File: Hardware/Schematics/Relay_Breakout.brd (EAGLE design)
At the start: 31 x 40 mm, 14 parts, among them J1 1X2-3.5MM, J2 1X2-3.5MM

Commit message: fixed some issues in relay breakout.
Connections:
- removed net N$2: D4.C, U$2.COIL1
- net +5V: now also D4.C, U$2.COIL1
- net PHASE_OUT: now also U$2.SWCLOSED; no longer U$2.SWOPEN
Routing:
- net +5V: track 56.9 -> 62.7 mm
- net N$2: track 2.60 -> 0.00 mm
- net PHASE: track 12.8 -> 14.7 mm
- net NULL: track 19.6 -> 20.9 mm
- added copper zone on layer 1, net NULL_OUT
- added copper zone on layer 1, net PHASE_OUT
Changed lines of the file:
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@@
 <autorouter>
 <pass name="Default">
-<param name="RoutingGrid" value="50mil"/>
+<param name="RoutingGrid" value="0.25mm"/>
 <param name="AutoGrid" value="1"/>
 <param name="Efforts" value="0"/>
 <param name="TopRouterVariant" value="1"/>
 <param name="tpViaShape" value="round"/>
-<param name="PrefDir.1" value="a"/>
+<param name="PrefDir.1" value="-"/>
 <param name="PrefDir.2" value="0"/>
 <param name="PrefDir.3" value="0"/>
@@
 <param name="PrefDir.14" value="0"/>
 <param name="PrefDir.15" value="0"/>
-<param name="PrefDir.16" value="a"/>
+<param name="PrefDir.16" value="|"/>
 <param name="cfVia" value="8"/>
 <param name="cfNonPref" value="5"/>
@@
 <signal name="PHASE_OUT">
 <contactref element="J2" pad="2"/>
-<contactref element="U$2" pad="SWOPEN"/>
-<polygon width="0.6096" layer="16" thermals="no">
-<vertex x="1.2" y="20.1"/>
-<vertex x="9.8" y="20.1"/>
-<vertex x="9.8" y="23.2"/>
-<vertex x="1.2" y="23.2"/>
+<contactref element="U$2" pad="SWCLOSED"/>
+<polygon width="0.4064" layer="16" thermals="no">
+<vertex x="2.2" y="20"/>
+<vertex x="1.2" y="20"/>
+<vertex x="1.2" y="33.3"/>
+<vertex x="9.4" y="33.3"/>
+<vertex x="9.4" y="28.2"/>
+<vertex x="4.2" y="23"/>
+<vertex x="4.2" y="20"/>
+</polygon>
+<polygon width="0.4064" layer="1" thermals="no">
+<vertex x="4.2" y="20"/>
+<vertex x="1.2" y="20"/>
+<vertex x="1.2" y="33.3"/>
+<vertex x="9.4" y="33.3"/>
+<vertex x="9.4" y="28.2"/>
+<vertex x="4.2" y="23"/>
 </polygon>
 </signal>
@@
 <wire x1="28.470734375" y1="26.7" x2="28.470734375" y2="26.804315625" width="1.016" layer="16"/>
 <wire x1="28.9" y1="26.6" x2="28.9" y2="20.7" width="2.54" layer="16"/>
-<wire x1="27.9" y1="26.7" x2="27.200734375" y2="26.804315625" width="0" layer="19" extent="16-16"/>
-<wire x1="28.9" y1="26.6" x2="28.470734375" y2="26.7" width="0" layer="19" extent="16-16"/>
+<wire x1="27.178" y1="26.797" x2="27.200734375" y2="26.804315625" width="0.127" layer="16"/>
+<wire x1="27.178" y1="26.797" x2="27.9" y2="26.7" width="0.127" layer="16"/>
+<wire x1="27.813" y1="20.574" x2="27.85" y2="20.54" width="0.127" layer="16"/>
+<wire x1="27.813" y1="20.574" x2="28.9" y2="20.7" width="0.127" layer="16"/>
 </signal>
 <signal name="NULL">
@@
 <wire x1="27.8" y1="16.2" x2="27.8" y2="11.6" width="3.81" layer="1"/>
 <wire x1="27.8" y1="11.6" x2="24" y2="11.6" width="3.81" layer="1"/>
-<wire x1="27.8" y1="11.6" x2="27.8" y2="11.6" width="0" layer="19" extent="1-16"/>
+<wire x1="22.86" y1="11.557" x2="24" y2="11.6" width="0.127" layer="1"/>
+<wire x1="22.86" y1="11.557" x2="22.77" y2="11.62" width="0.127" layer="1"/>
 </signal>
 <signal name="N$24">
@@
 <wire x1="27.9" y1="30.5" x2="18.5" y2="30.5" width="0.6096" layer="1"/>
 <wire x1="18.5" y1="30.5" x2="18.6" y2="30.4" width="0.6096" layer="1"/>
-<wire x1="18.6" y1="30.4" x2="18.6" y2="4.4" width="0.6096" layer="1"/>
+<wire x1="18.6" y1="30.4" x2="18.6" y2="23" width="0.6096" layer="1"/>
+<wire x1="18.6" y1="23" x2="18.6" y2="4.4" width="0.6096" layer="1"/>
 <wire x1="18.6" y1="4.4" x2="17.62" y2="3.42" width="0.6096" layer="1"/>
 <wire x1="17.62" y1="3.42" x2="17.62" y2="2.42" width="0.6096" layer="1"/>
+<contactref element="U$2" pad="COIL1"/>
+<contactref element="D4" pad="C"/>
+<wire x1="20.77" y1="20.8" x2="20.155" y2="21.415" width="0.6096" layer="16"/>
+<wire x1="20.155" y1="21.415" x2="18.42" y2="21.415" width="0.6096" layer="16"/>
+<wire x1="20.8" y1="20.8" x2="18.6" y2="23" width="0.6096" layer="1"/>
+<wire x1="20.828" y1="20.828" x2="20.77" y2="20.8" width="0.127" layer="1"/>
+<wire x1="20.828" y1="20.828" x2="20.8" y2="20.8" width="0.127" layer="1"/>
 </signal>
 <signal name="N$41">
@@
 <vertex x="9.8" y="14.5"/>
 <vertex x="1.3" y="14.5"/>
+</polygon>
+<polygon width="0.4064" layer="1" thermals="no">
+<vertex x="2.2" y="18.3"/>
+<vertex x="9.9" y="18.3"/>
+<vertex x="9.9" y="14.4"/>
+<vertex x="1.2" y="14.4"/>
+<vertex x="1.2" y="18.3"/>
 </polygon>
 </signal>
@@
 <wire x1="20.81" y1="32.84" x2="20.81" y2="34.54" width="0.6096" layer="16"/>
 </signal>
-<signal name="N$2">
-<contactref element="U$2" pad="COIL1"/>
-<contactref element="D4" pad="C"/>
-<wire x1="20.77" y1="20.8" x2="20.155" y2="21.415" width="0.6096" layer="16"/>
-<wire x1="20.155" y1="21.415" x2="18.42" y2="21.415" width="0.6096" layer="16"/>
-</signal>
 </signals>

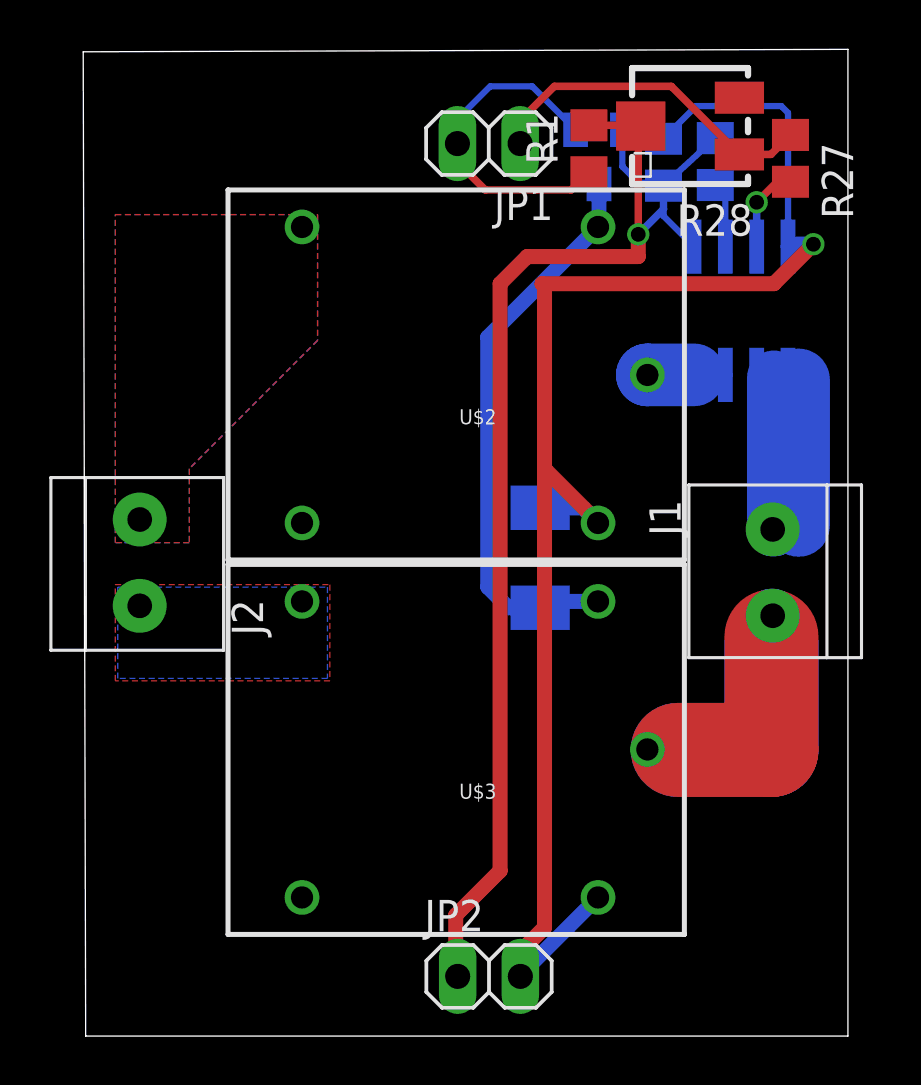
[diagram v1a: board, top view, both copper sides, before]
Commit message: Routed power socket board.
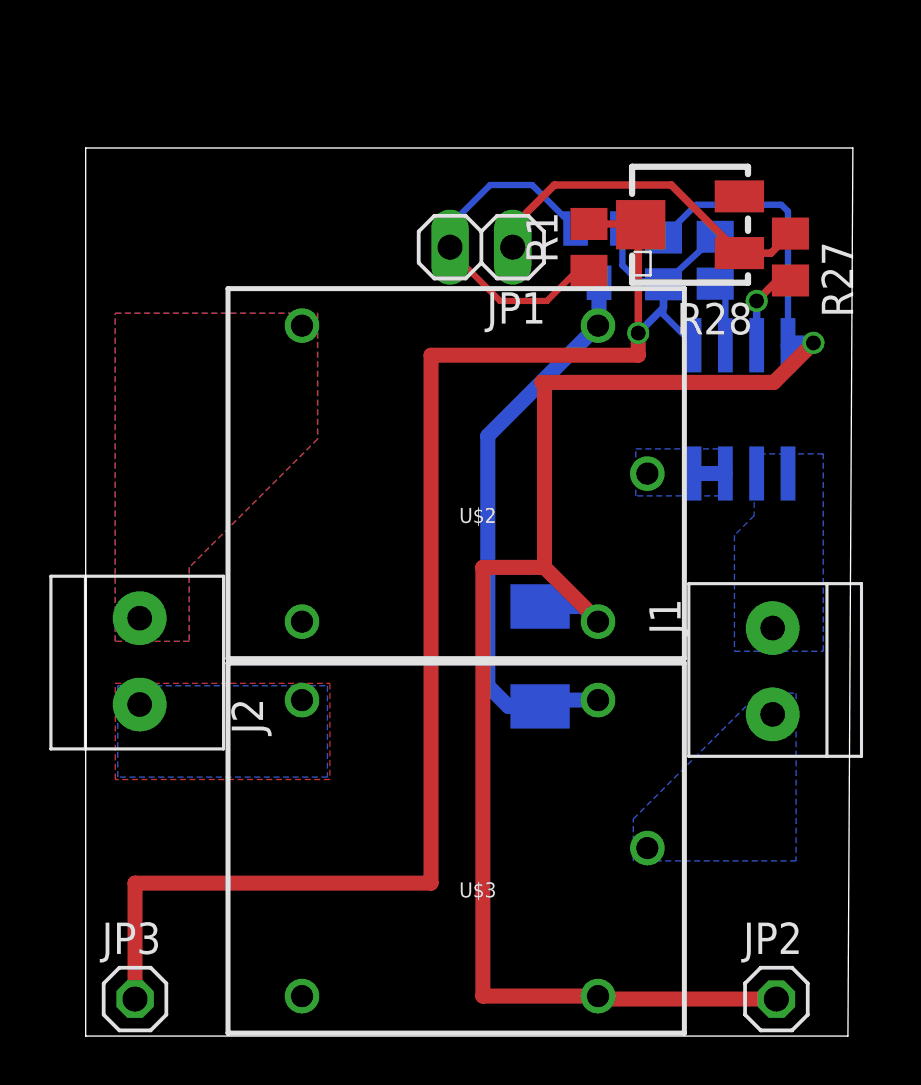
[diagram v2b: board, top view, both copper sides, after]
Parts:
- added JP3: (no value), pinhead:1X01
- JP2: device pinhead:1X02 -> pinhead:1X01
- moved JP2 11.7 mm to (28.0, 1.50)
- moved JP1 4.21 mm to (16.0, 32.0)
- moved C7 4.00 mm to (23.4, 31.4)
- moved C8 4.00 mm to (25.5, 31.4)
- moved AMP1 4.00 mm to (26.6, 25.4)
- moved D4 4.00 mm to (18.4, 15.4)
- moved Q1 4.00 mm to (20.8, 31.6)
- moved R1 4.00 mm to (20.4, 32.0)
- moved R27 4.00 mm to (28.6, 31.6)
- moved R28 4.00 mm to (24.5, 32.9)
- moved U$2 4.00 mm to (15.4, 22.7)
- moved U$3 4.00 mm to (15.4, 7.50)
- moved J1 4.00 mm to (27.9, 14.7)
- moved J2 4.00 mm to (2.19, 15.2)
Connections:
- net +5V: now also JP2.1; no longer JP2.2
- net GND: now also JP3.1; no longer JP2.1
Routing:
- net NULL: track 20.9 -> 0.00 mm
- net PHASE: track 14.7 -> 0.00 mm
- net GND: track 54.1 -> 65.7 mm
- net +5V: track 62.7 -> 69.1 mm
- net PHASE1: track 3.17 -> 1.27 mm
- net GATE: track 13.9 -> 14.7 mm
- added copper zone on layer 16, net NULL
- added copper zone on layer 16, net PHASE
- added copper zone on layer 16, net PHASE1
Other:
- board size 31 x 40 mm -> 31.1 x 36 mm

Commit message: Added relay breakout panelizing config.
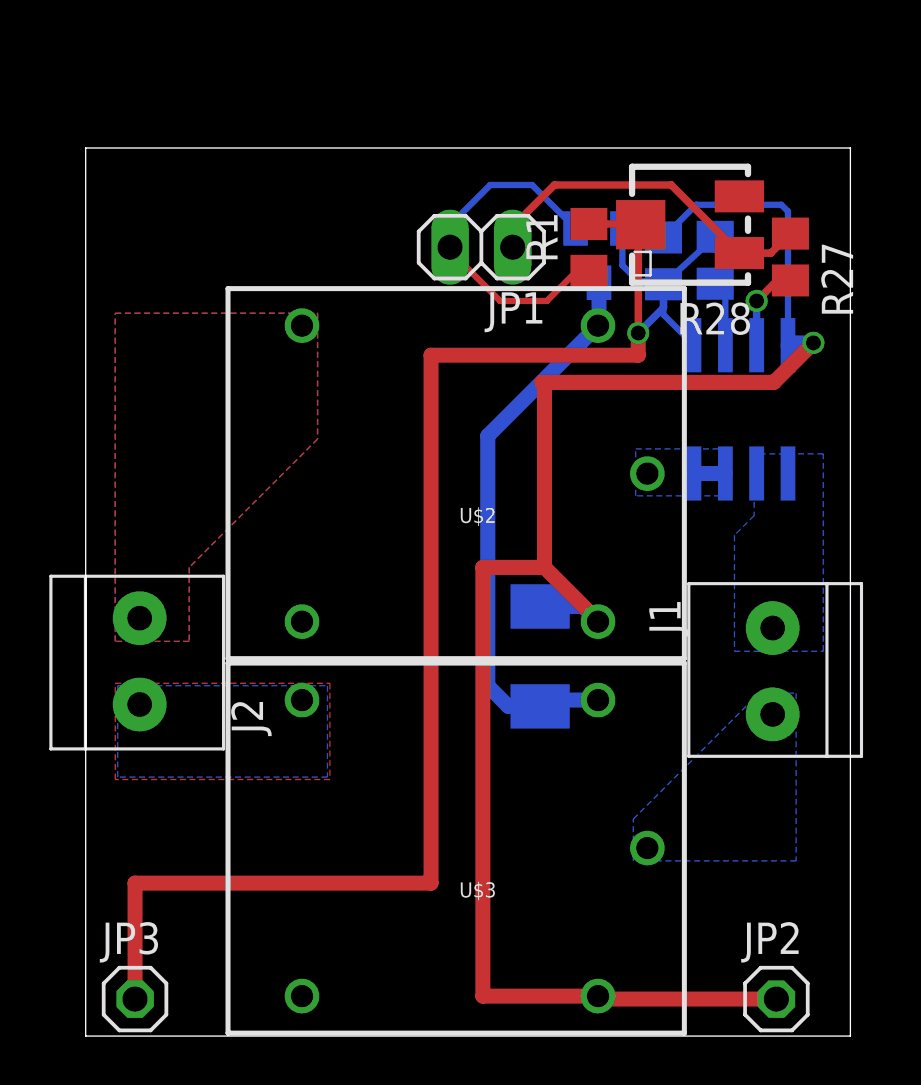
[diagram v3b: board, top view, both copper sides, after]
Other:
- board size 31.1 x 36 mm -> 31 x 36 mm
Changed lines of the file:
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@@
 <board>
 <plain>
-<wire x1="0" y1="0" x2="30.9" y2="0" width="0" layer="20"/>
-<wire x1="30.9" y1="0" x2="31.1" y2="36" width="0" layer="20"/>
-<wire x1="31.1" y1="36" x2="0" y2="36" width="0" layer="20"/>
+<wire x1="0" y1="0" x2="31" y2="0" width="0" layer="20"/>
+<wire x1="31" y1="0" x2="31" y2="36" width="0" layer="20"/>
+<wire x1="31" y1="36" x2="0" y2="36" width="0" layer="20"/>
 <wire x1="0" y1="36" x2="0" y2="0" width="0" layer="20"/>
 </plain>

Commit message: Added voltage regulators to both boards. Removed solder mask en 220V traces.
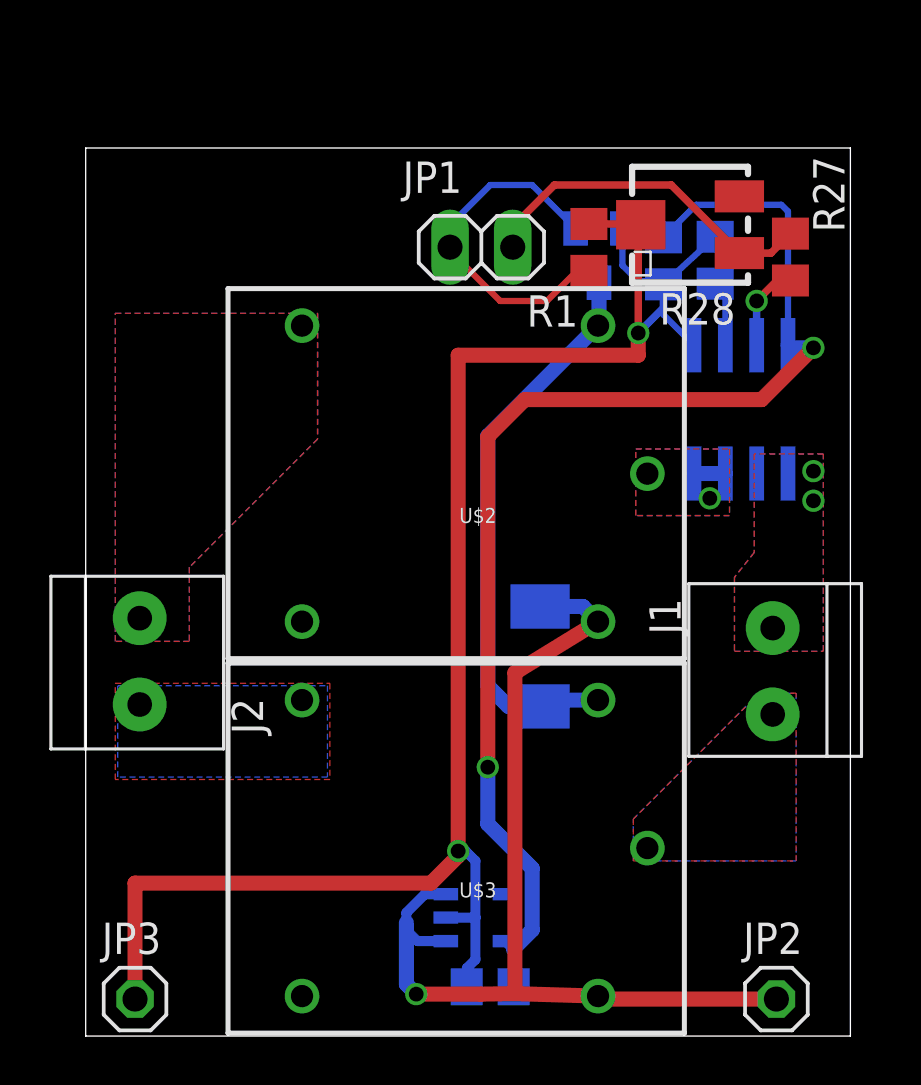
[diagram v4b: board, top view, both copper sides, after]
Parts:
- added 4.5V_REG: S1112, PowerSocket:SOT23-5
- added C1: 470nF, rcl:C0805
- R28: value 10K -> 20K
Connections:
- new net 4.5V: 4.5V_REG.5, AMP1.8, C1.2, C7.1
- net +5V: now also 4.5V_REG.1, 4.5V_REG.3; no longer AMP1.8, C7.1
- net GND: now also 4.5V_REG.2, C1.1
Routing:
- net 4.5V: track 0.00 -> 50.7 mm, vias 0 -> 2
- net +5V: track 69.1 -> 41.9 mm
- net GND: track 65.7 -> 72.3 mm, vias 1 -> 2
- net PHASE1: vias 0 -> 1
- added copper zone on layer 1, net NULL
- added copper zone on layer 1, net PHASE
- added copper zone on layer 1, net PHASE1

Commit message: Updated software to esp32.
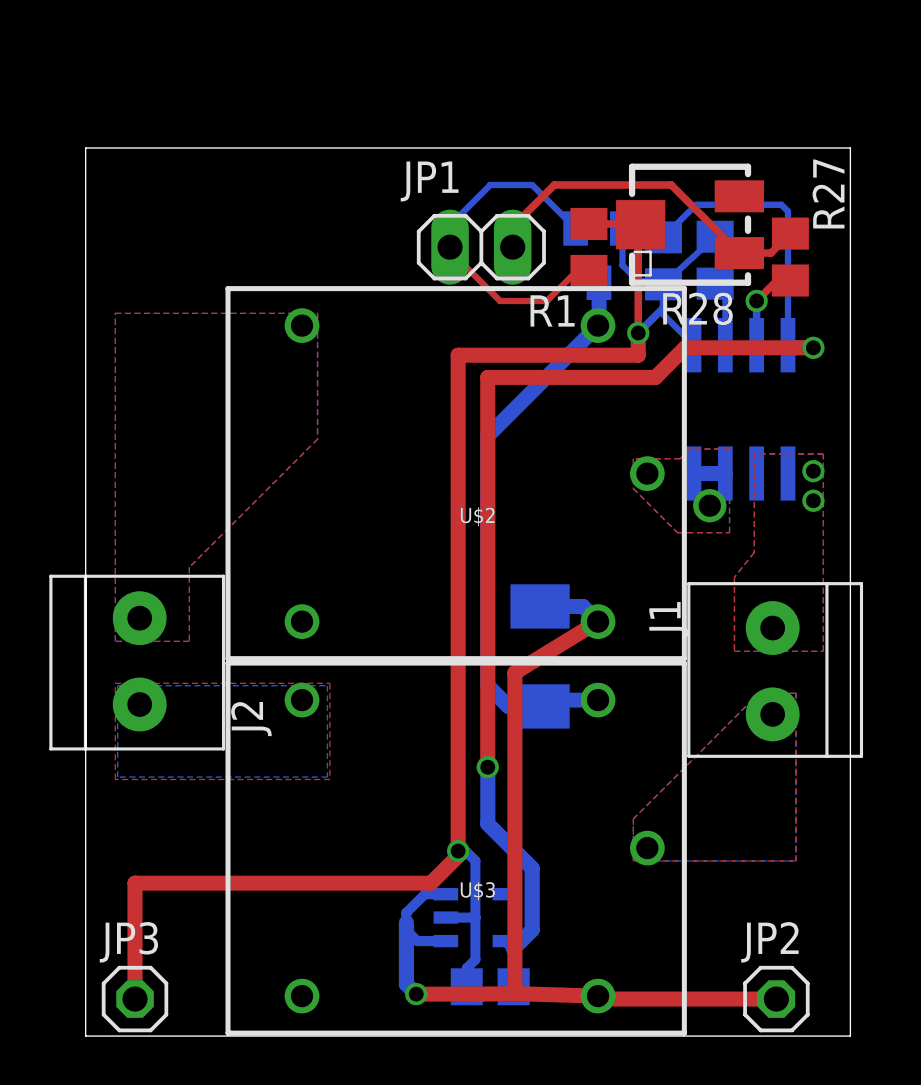
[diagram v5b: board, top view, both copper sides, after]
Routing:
- net 4.5V: track 50.7 -> 52.2 mm
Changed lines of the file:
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@@
 <setting verticaltext="up"/>
 </settings>
-<grid distance="3.93700787" unitdist="mil" unit="mil" style="lines" multiple="1" display="no" altdistance="0.1" altunitdist="mm" altunit="mm"/>
+<grid distance="0.1" unitdist="mm" unit="mm" style="lines" multiple="1" display="no" altdistance="0.1" altunitdist="mm" altunit="mm"/>
 <layers>
 <layer number="1" name="Top" color="4" fill="1" visible="yes" active="yes"/>
@@
 <layer number="17" name="Pads" color="2" fill="1" visible="yes" active="yes"/>
 <layer number="18" name="Vias" color="2" fill="1" visible="yes" active="yes"/>
-<layer number="19" name="Unrouted" color="6" fill="1" visible="no" active="yes"/>
+<layer number="19" name="Unrouted" color="6" fill="1" visible="yes" active="yes"/>
 <layer number="20" name="Dimension" color="15" fill="1" visible="yes" active="yes"/>
 <layer number="21" name="tPlace" color="7" fill="1" visible="yes" active="yes"/>
@@
 <layer number="27" name="tValues" color="7" fill="1" visible="no" active="yes"/>
 <layer number="28" name="bValues" color="7" fill="1" visible="no" active="yes"/>
-<layer number="29" name="tStop" color="7" fill="3" visible="no" active="yes"/>
+<layer number="29" name="tStop" color="7" fill="3" visible="yes" active="yes"/>
 <layer number="30" name="bStop" color="7" fill="6" visible="yes" active="yes"/>
 <layer number="31" name="tCream" color="7" fill="4" visible="no" active="yes"/>
@@
 </polygon>
 <polygon width="0.4064" layer="29">
-<vertex x="26.1" y="23.8"/>
-<vertex x="22.3" y="23.8"/>
-<vertex x="22.3" y="21.1"/>
-<vertex x="26.1" y="21.1"/>
-<vertex x="26.1" y="23.7"/>
-</polygon>
-<polygon width="0.4064" layer="29">
 <vertex x="9.4" y="29.3"/>
 <vertex x="1.2" y="29.3"/>
@@
 </polygon>
 <polygon width="0.4064" layer="30">
-<vertex x="26.1" y="21.1"/>
 <vertex x="26.1" y="23.8"/>
-<vertex x="22.3" y="23.8"/>
-<vertex x="22.3" y="21.1"/>
+<vertex x="24.5" y="23.8"/>
+<vertex x="24.1" y="23.4"/>
+<vertex x="22.2" y="23.4"/>
+<vertex x="22.2" y="22.2"/>
+<vertex x="24" y="20.4"/>
+<vertex x="26.1" y="20.4"/>
+</polygon>
+<polygon width="0.4064" layer="29">
+<vertex x="26.1" y="23.8"/>
+<vertex x="24.5" y="23.8"/>
+<vertex x="24.1" y="23.4"/>
+<vertex x="22.2" y="23.4"/>
+<vertex x="22.2" y="22.2"/>
+<vertex x="24" y="20.4"/>
+<vertex x="26.1" y="20.4"/>
 </polygon>
 </plain>
@@
 <wire x1="14.8" y1="31.8" x2="14.77" y2="31.8" width="0.254" layer="1"/>
 <wire x1="14.77" y1="31.8" x2="14.77" y2="31.98" width="0.254" layer="1"/>
-<wire x1="20.4" y1="31" x2="20.4" y2="31.02" width="0" layer="19" extent="1-1"/>
+<wire x1="20.4" y1="31" x2="20.4" y2="31.02" width="0.6096" layer="1"/>
 </signal>
 <signal name="AMP">
@@
 <contactref element="AMP1" pad="4"/>
 <wire x1="24.660734375" y1="22.804315625" x2="25.930734375" y2="22.804315625" width="0.6096" layer="16"/>
-<polygon width="0.4064" layer="16" thermals="no">
-<vertex x="26.1" y="21.1"/>
-<vertex x="22.3" y="21.1"/>
-<vertex x="22.3" y="23.8"/>
-<vertex x="26.1" y="23.8"/>
-</polygon>
+<via x="25.3" y="21.5" extent="1-16" drill="0.9" shape="square"/>
 <polygon width="0.4064" layer="1" thermals="no">
 <vertex x="26.1" y="23.8"/>
-<vertex x="26.1" y="21.1"/>
-<vertex x="22.3" y="21.1"/>
-<vertex x="22.3" y="23.8"/>
-</polygon>
-<via x="25.3" y="21.8" extent="1-16" drill="0.6" shape="square"/>
+<vertex x="24.5" y="23.8"/>
+<vertex x="24.1" y="23.4"/>
+<vertex x="22.2" y="23.4"/>
+<vertex x="22.2" y="22.2"/>
+<vertex x="24" y="20.4"/>
+<vertex x="26.1" y="20.4"/>
+</polygon>
+<polygon width="0.4064" layer="16" thermals="no">
+<vertex x="26.1" y="23.8"/>
+<vertex x="24.5" y="23.8"/>
+<vertex x="24.1" y="23.4"/>
+<vertex x="22.2" y="23.4"/>
+<vertex x="22.2" y="22.2"/>
+<vertex x="24" y="20.4"/>
+<vertex x="26" y="20.4"/>
+<vertex x="26.1" y="20.4"/>
+</polygon>
 </signal>
 <signal name="PHASE_OUT">
@@
 <wire x1="28.470734375" y1="33.429265625" x2="28.470734375" y2="28.004315625" width="0.254" layer="16"/>
 <wire x1="28.470734375" y1="28.004315625" x2="28.57505" y2="27.9" width="0.6096" layer="16"/>
-<wire x1="28.57505" y1="27.9" x2="29.5" y2="27.9" width="0.6096" layer="16"/>
 <via x="29.5" y="27.9" extent="1-16" drill="0.6" shape="square"/>
-<wire x1="29.5" y1="27.9" x2="27.4" y2="25.8" width="0.6096" layer="1"/>
 <wire x1="17" y1="3.85" x2="17.35" y2="3.5" width="0.4064" layer="16"/>
 <wire x1="17.35" y1="3.5" x2="17.35" y2="2" width="0.4064" layer="16"/>
@@
 <wire x1="16.3" y1="8.6" x2="16.3" y2="10.9" width="0.6096" layer="16"/>
 <via x="16.3" y="10.9" extent="1-16" drill="0.6" shape="square"/>
-<wire x1="16.3" y1="10.9" x2="16.3" y2="24.3" width="0.6096" layer="1"/>
-<wire x1="16.3" y1="24.3" x2="17.8" y2="25.8" width="0.6096" layer="1"/>
-<wire x1="17.8" y1="25.8" x2="27.4" y2="25.8" width="0.6096" layer="1"/>
+<wire x1="16.3" y1="10.9" x2="16.3" y2="26.7" width="0.6096" layer="1"/>
+<wire x1="16.3" y1="26.7" x2="23.1" y2="26.7" width="0.6096" layer="1"/>
+<wire x1="23.1" y1="26.7" x2="24.3" y2="27.9" width="0.6096" layer="1"/>
+<wire x1="24.3" y1="27.9" x2="29.5" y2="27.9" width="0.6096" layer="1"/>
+<wire x1="28.57505" y1="27.9" x2="29.5" y2="27.9" width="0.6096" layer="16"/>
 </signal>
 </signals>
